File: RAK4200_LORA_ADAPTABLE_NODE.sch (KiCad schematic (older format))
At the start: 14 parts, among them J1 Screw_Terminal_01x03, J2 Screw_Terminal_01x03, J3 Conn_01x11_Male, J4 Conn_01x11_Male, J5 Conn_01x01_Male, U1 RAK4200

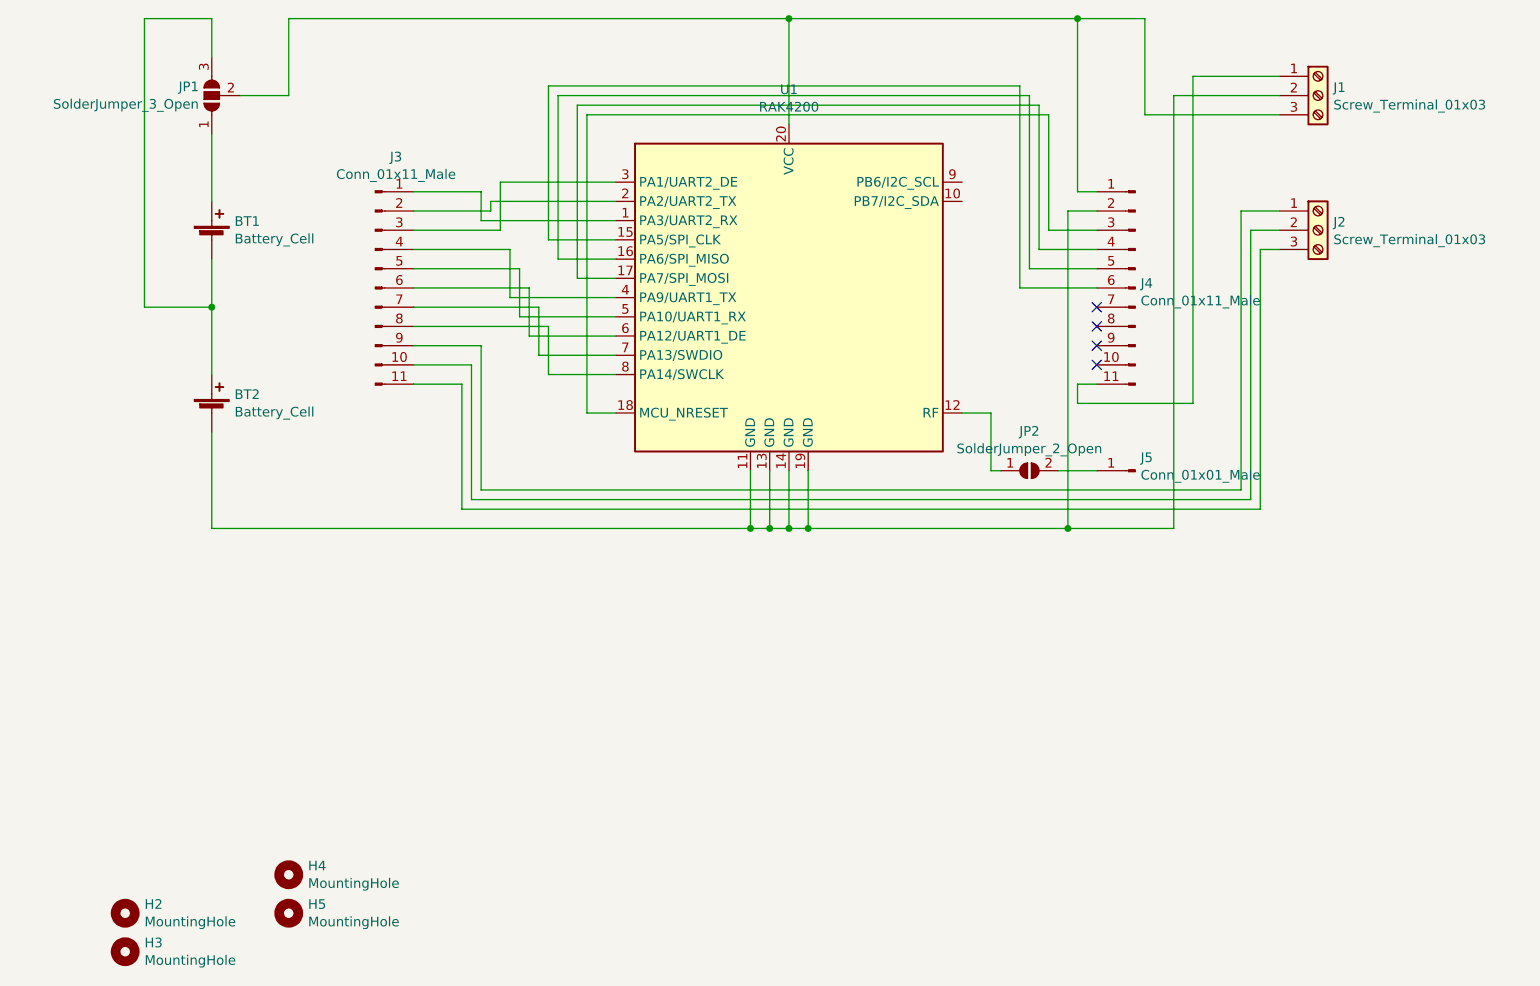
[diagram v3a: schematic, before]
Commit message: all traces routed
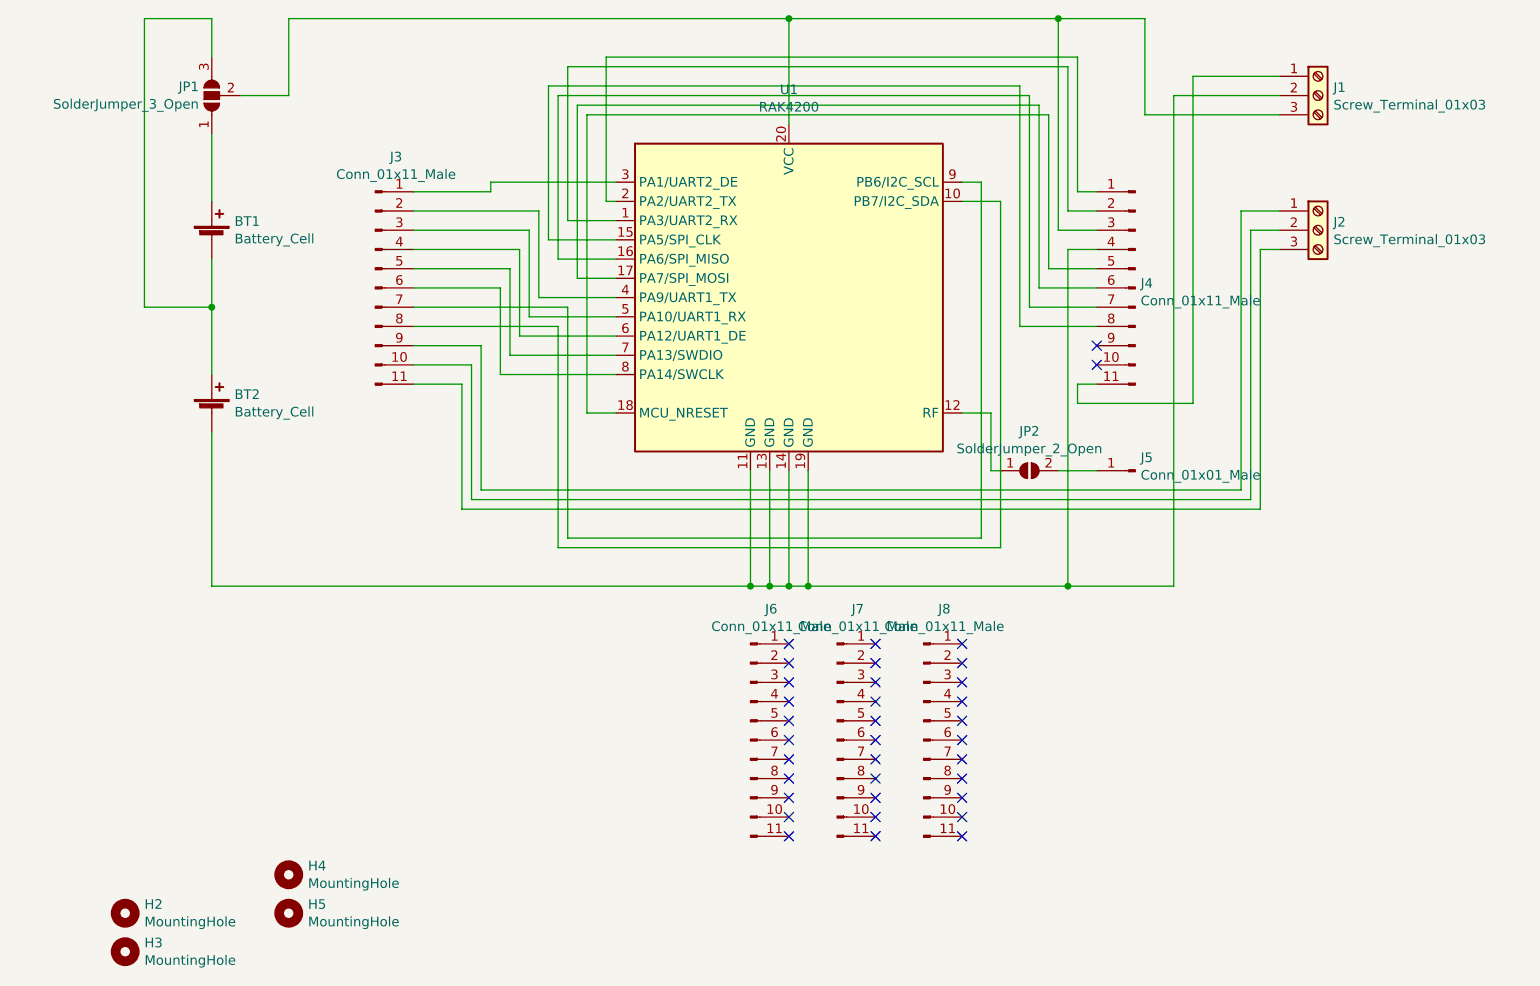
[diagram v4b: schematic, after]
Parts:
- added J6, J7, J8: Conn_01x11_Male, Connector_PinHeader_2.54mm:PinHeader_1x11_P2.54mm_Vertical, symbol Connector:Conn_01x11_Male
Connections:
- net at U1.1 (PA3/UART2_RX): now also J4.2 (Pin_2); no longer J3.1 (Pin_1)
- net at U1.10 (PB7/I2C_SDA): now also J3.8 (Pin_8)
- net at BT2.2 (-), J1.2 (Pin_2), U1.11 (GND)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: now also J4.4 (Pin_4); no longer J4.2 (Pin_2)
- net at U1.15 (PA5/SPI_CLK): now also J4.8 (Pin_8); no longer J4.6 (Pin_6)
- net at U1.16 (PA6/SPI_MISO): now also J4.7 (Pin_7); no longer J4.5 (Pin_5)
- net at U1.17 (PA7/SPI_MOSI): now also J4.6 (Pin_6); no longer J4.4 (Pin_4)
- net at U1.18 (MCU_NRESET): now also J4.5 (Pin_5); no longer J4.3 (Pin_3)
- net at U1.2 (PA2/UART2_TX): now also J4.1 (Pin_1); no longer J3.2 (Pin_2)
- net at J1.3 (Pin_3), JP1.2 (C), U1.20 (VCC): now also J4.3 (Pin_3); no longer J4.1 (Pin_1)
- net at U1.3 (PA1/UART2_DE): now also J3.1 (Pin_1); no longer J3.3 (Pin_3)
- net at U1.4 (PA9/UART1_TX): now also J3.2 (Pin_2); no longer J3.4 (Pin_4)
- net at U1.5 (PA10/UART1_RX): now also J3.3 (Pin_3); no longer J3.5 (Pin_5)
- net at U1.6 (PA12/UART1_DE): now also J3.4 (Pin_4); no longer J3.6 (Pin_6)
- net at U1.7 (PA13/SWDIO): now also J3.5 (Pin_5); no longer J3.7 (Pin_7)
- net at U1.8 (PA14/SWCLK): now also J3.6 (Pin_6); no longer J3.8 (Pin_8)
- net at U1.9 (PB6/I2C_SCL): now also J3.7 (Pin_7)
- no-connect marks 4 -> 35
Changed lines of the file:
@@
 encoding utf-8
 Sheet 1 1
-Title ""
+Title "RAK4200 LORA ADAPTABLE NODE"
 Date ""
 Rev ""
-Comp ""
+Comp "Galopago"
 Comment1 ""
 Comment2 ""
@@
 	2650 3300 2650 3550
 Wire Wire Line
-	2650 4200 2650 4700
-Wire Wire Line
-	2650 4700 5450 4700
-Wire Wire Line
-	5450 4700 5450 4400
+	2650 4200 2650 5000
+Wire Wire Line
+	2650 5000 5450 5000
+Wire Wire Line
+	5450 5000 5450 4400
 Wire Wire Line
 	2800 2450 3050 2450
@@
 $EndComp
 Wire Wire Line
-	5550 4400 5550 4700
-Wire Wire Line
-	5550 4700 5450 4700
-Connection ~ 5450 4700
-Wire Wire Line
-	5650 4400 5650 4700
-Wire Wire Line
-	5650 4700 5550 4700
-Connection ~ 5550 4700
-Wire Wire Line
-	5750 4400 5750 4700
-Wire Wire Line
-	5750 4700 5650 4700
-Connection ~ 5650 4700
+	5550 4400 5550 5000
+Wire Wire Line
+	5550 5000 5450 5000
+Connection ~ 5450 5000
+Wire Wire Line
+	5650 4400 5650 5000
+Wire Wire Line
+	5650 5000 5550 5000
+Connection ~ 5550 5000
+Wire Wire Line
+	5750 4400 5750 5000
+Wire Wire Line
+	5750 5000 5650 5000
+Connection ~ 5650 5000
 Wire Wire Line
 	8200 2450 7650 2450
 Wire Wire Line
-	7650 2450 7650 4700
-Wire Wire Line
-	7650 4700 7100 4700
-Connection ~ 5750 4700
+	7650 2450 7650 5000
+Wire Wire Line
+	7650 5000 7100 5000
+Connection ~ 5750 5000
 Wire Wire Line
 	8200 2550 7500 2550
@@
 	7500 2550 7500 2050
 Wire Wire Line
-	7500 2050 7150 2050
+	7500 2050 7050 2050
 Connection ~ 5650 2050
 $Comp
@@
 Wire Wire Line
 	6700 4100 6550 4100
-Wire Wire Line
-	7250 2950 7150 2950
-Wire Wire Line
-	7150 2950 7150 2050
-Connection ~ 7150 2050
-Wire Wire Line
-	7150 2050 5650 2050
-Wire Wire Line
-	7250 3050 7100 3050
-Wire Wire Line
-	7100 3050 7100 4700
-Connection ~ 7100 4700
-Wire Wire Line
-	7100 4700 5750 4700
-Wire Wire Line
-	7250 3150 7000 3150
-Wire Wire Line
-	7000 3150 7000 2550
+Connection ~ 7050 2050
+Wire Wire Line
+	7050 2050 5650 2050
+Connection ~ 7100 5000
+Wire Wire Line
+	7100 5000 5750 5000
 Wire Wire Line
 	7000 2550 4600 2550
@@
 	4600 4100 4750 4100
 Wire Wire Line
-	7250 3250 6950 3250
-Wire Wire Line
-	6950 3250 6950 2500
-Wire Wire Line
 	6950 2500 4550 2500
 Wire Wire Line
@@
 	4550 3400 4750 3400
 Wire Wire Line
-	7250 3350 6900 3350
-Wire Wire Line
-	6900 3350 6900 2450
-Wire Wire Line
 	6900 2450 4450 2450
 Wire Wire Line
@@
 	4450 3300 4750 3300
 Wire Wire Line
-	7250 3450 6850 3450
-Wire Wire Line
-	6850 3450 6850 2400
-Wire Wire Line
 	6850 2400 4400 2400
 Wire Wire Line
@@
 	4400 3200 4750 3200
 Wire Wire Line
-	4750 3100 4050 3100
-Wire Wire Line
-	4050 3100 4050 2950
-Wire Wire Line
-	4050 2950 3700 2950
-Wire Wire Line
-	4750 3000 4100 3000
-Wire Wire Line
-	4100 3000 4100 3050
-Wire Wire Line
-	4100 3050 3700 3050
-Wire Wire Line
-	4750 2900 4150 2900
-Wire Wire Line
-	4150 2900 4150 3150
-Wire Wire Line
-	4150 3150 3700 3150
-Wire Wire Line
-	4750 3500 4200 3500
-Wire Wire Line
-	4200 3500 4200 3250
-Wire Wire Line
-	4200 3250 3700 3250
-Wire Wire Line
-	4750 3600 4250 3600
-Wire Wire Line
-	4250 3600 4250 3350
-Wire Wire Line
-	4250 3350 3700 3350
-Wire Wire Line
-	4750 3700 4300 3700
-Wire Wire Line
-	4300 3700 4300 3450
-Wire Wire Line
-	4300 3450 3700 3450
-Wire Wire Line
-	4750 3800 4350 3800
-Wire Wire Line
-	4350 3800 4350 3550
-Wire Wire Line
-	4350 3550 3700 3550
-Wire Wire Line
-	4750 3900 4400 3900
-Wire Wire Line
-	4400 3900 4400 3650
-Wire Wire Line
-	4400 3650 3700 3650
-Wire Wire Line
-	8200 2350 7750 2350
-Wire Wire Line
 	7750 2350 7750 4050
 Wire Wire Line
@@
 Wire Wire Line
 	4050 3750 3700 3750
-NoConn ~ 7250 3550
-NoConn ~ 7250 3650
 NoConn ~ 7250 3750
 NoConn ~ 7250 3850
+Wire Wire Line
+	7250 3650 6850 3650
+Wire Wire Line
+	6850 2400 6850 3650
+Wire Wire Line
+	7250 3550 6900 3550
+Wire Wire Line
+	6900 2450 6900 3550
+Wire Wire Line
+	7250 3450 6950 3450
+Wire Wire Line
+	6950 2500 6950 3450
+Wire Wire Line
+	7250 3350 7000 3350
+Wire Wire Line
+	7000 2550 7000 3350
+Wire Wire Line
+	7250 3250 7100 3250
+Wire Wire Line
+	7100 3250 7100 5000
+Wire Wire Line
+	8200 2350 7750 2350
+Wire Wire Line
+	7250 3150 7050 3150
+Wire Wire Line
+	7050 2050 7050 3150
+Wire Wire Line
+	6550 3000 6750 3000
+Wire Wire Line
+	6750 4800 4450 4800
+Wire Wire Line
+	4450 4800 4450 3650
+Wire Wire Line
+	4450 3650 3700 3650
+Wire Wire Line
+	6750 3000 6750 4800
+Wire Wire Line
+	6550 2900 6650 2900
+Wire Wire Line
+	6650 2900 6650 4750
+Wire Wire Line
+	6650 4750 4500 4750
+Wire Wire Line
+	4500 4750 4500 3550
+Wire Wire Line
+	4500 3550 3700 3550
+Wire Wire Line
+	4750 3900 4150 3900
+Wire Wire Line
+	4150 3900 4150 3450
+Wire Wire Line
+	4150 3450 3700 3450
+Wire Wire Line
+	4750 3800 4200 3800
+Wire Wire Line
+	4200 3800 4200 3350
+Wire Wire Line
+	4200 3350 3700 3350
+Wire Wire Line
+	4750 3700 4250 3700
+Wire Wire Line
+	4250 3700 4250 3250
+Wire Wire Line
+	4250 3250 3700 3250
+Wire Wire Line
+	4750 3600 4300 3600
+Wire Wire Line
+	4300 3600 4300 3150
+Wire Wire Line
+	4300 3150 3700 3150
+Wire Wire Line
+	4750 3500 4350 3500
+Wire Wire Line
+	4350 3500 4350 3050
+Wire Wire Line
+	4350 3050 3700 3050
+Wire Wire Line
+	4750 2900 4100 2900
+Wire Wire Line
+	4100 2900 4100 2950
+Wire Wire Line
+	4100 2950 3700 2950
+Wire Wire Line
+	4750 3100 4500 3100
+Wire Wire Line
+	4500 3100 4500 2300
+Wire Wire Line
+	4500 2300 7100 2300
+Wire Wire Line
+	7100 2300 7100 3050
+Wire Wire Line
+	7100 3050 7250 3050
+Wire Wire Line
+	4750 3000 4700 3000
+Wire Wire Line
+	4700 3000 4700 2250
+Wire Wire Line
+	4700 2250 7150 2250
+Wire Wire Line
+	7150 2250 7150 2950
+Wire Wire Line
+	7150 2950 7250 2950
+$Comp
+L Connector:Conn_01x11_Male J6
+U 1 1 5F28B36C
+P 5450 5800
+F 0 "J6" H 5558 6481 50  0000 C CNN
+F 1 "Conn_01x11_Male" H 5558 6390 50  0000 C CNN
+F 2 "Connector_PinHeader_2.54mm:PinHeader_1x11_P2.54mm_Vertical" H 5450 5800 50  0001 C CNN
+F 3 "~" H 5450 5800 50  0001 C CNN
+	1    5450 5800
+	1    0    0    -1
+$EndComp
+$Comp
+L Connector:Conn_01x11_Male J7
+U 1 1 5F28CF39
+P 5900 5800
+F 0 "J7" H 6008 6481 50  0000 C CNN
+F 1 "Conn_01x11_Male" H 6008 6390 50  0000 C CNN
+F 2 "Connector_PinHeader_2.54mm:PinHeader_1x11_P2.54mm_Vertical" H 5900 5800 50  0001 C CNN
+F 3 "~" H 5900 5800 50  0001 C CNN
+	1    5900 5800
+	1    0    0    -1
+$EndComp
+$Comp
+L Connector:Conn_01x11_Male J8
+U 1 1 5F28EB9D
+P 6350 5800
+F 0 "J8" H 6458 6481 50  0000 C CNN
+F 1 "Conn_01x11_Male" H 6458 6390 50  0000 C CNN
+F 2 "Connector_PinHeader_2.54mm:PinHeader_1x11_P2.54mm_Vertical" H 6350 5800 50  0001 C CNN
+F 3 "~" H 6350 5800 50  0001 C CNN
+	1    6350 5800
+	1    0    0    -1
+$EndComp
+NoConn ~ 5650 5300
+NoConn ~ 5650 5400
+NoConn ~ 5650 5500
+NoConn ~ 5650 5600
+NoConn ~ 5650 5700
+NoConn ~ 5650 5800
+NoConn ~ 5650 5900
+NoConn ~ 5650 6000
+NoConn ~ 5650 6100
+NoConn ~ 5650 6200
+NoConn ~ 5650 6300
+NoConn ~ 6100 6300
+NoConn ~ 6100 6200
+NoConn ~ 6100 6100
+NoConn ~ 6100 6000
+NoConn ~ 6100 5900
+NoConn ~ 6100 5800
+NoConn ~ 6100 5700
+NoConn ~ 6100 5600
+NoConn ~ 6100 5500
+NoConn ~ 6100 5400
+NoConn ~ 6100 5300
+NoConn ~ 6550 5300
+NoConn ~ 6550 5400
+NoConn ~ 6550 5500
+NoConn ~ 6550 5600
+NoConn ~ 6550 5700
+NoConn ~ 6550 5800
+NoConn ~ 6550 5900
+NoConn ~ 6550 6000
+NoConn ~ 6550 6100
+NoConn ~ 6550 6200
+NoConn ~ 6550 6300
 $EndSCHEMATC
